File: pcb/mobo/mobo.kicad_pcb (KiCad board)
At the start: 2 copper layers, 51.6 x 89 mm, 69 parts, among them J1 SWD_10, J2 PEEL_MOTOR, J3 DRIVE_MOTOR, J4 SW1, J5 SPRING_FINGERS, J6 SW2, J7 SW1, J8 USART1, J9 SWD_10, U1 STM32F031C6Tx, U2 STM32F031K6Ux, U4 AP1117-33, U5 MC34063AD, U6 MAX3078E, U7 DRV8837, U8 DRV8837, Y1 8MHz

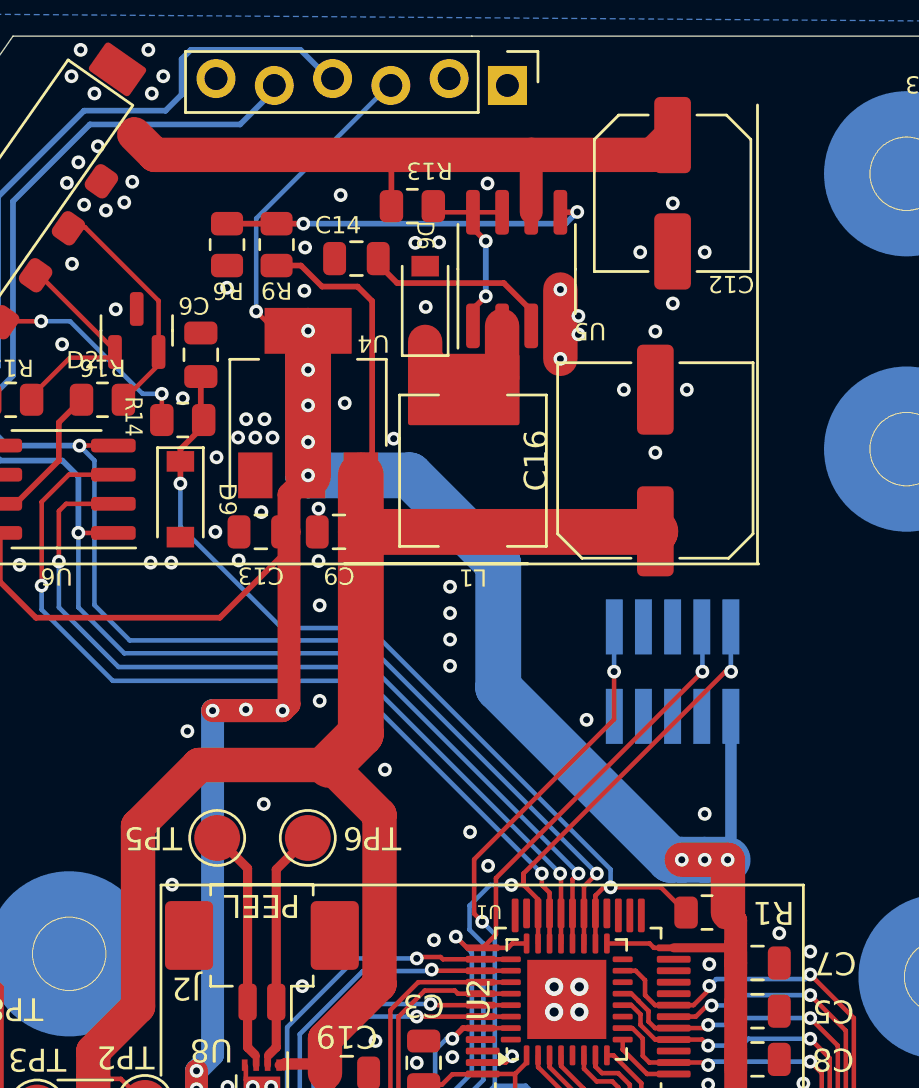
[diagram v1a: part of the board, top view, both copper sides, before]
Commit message: Convert SWD connector on back to TC2030. Left one on front for Adafruit 5434 connector.
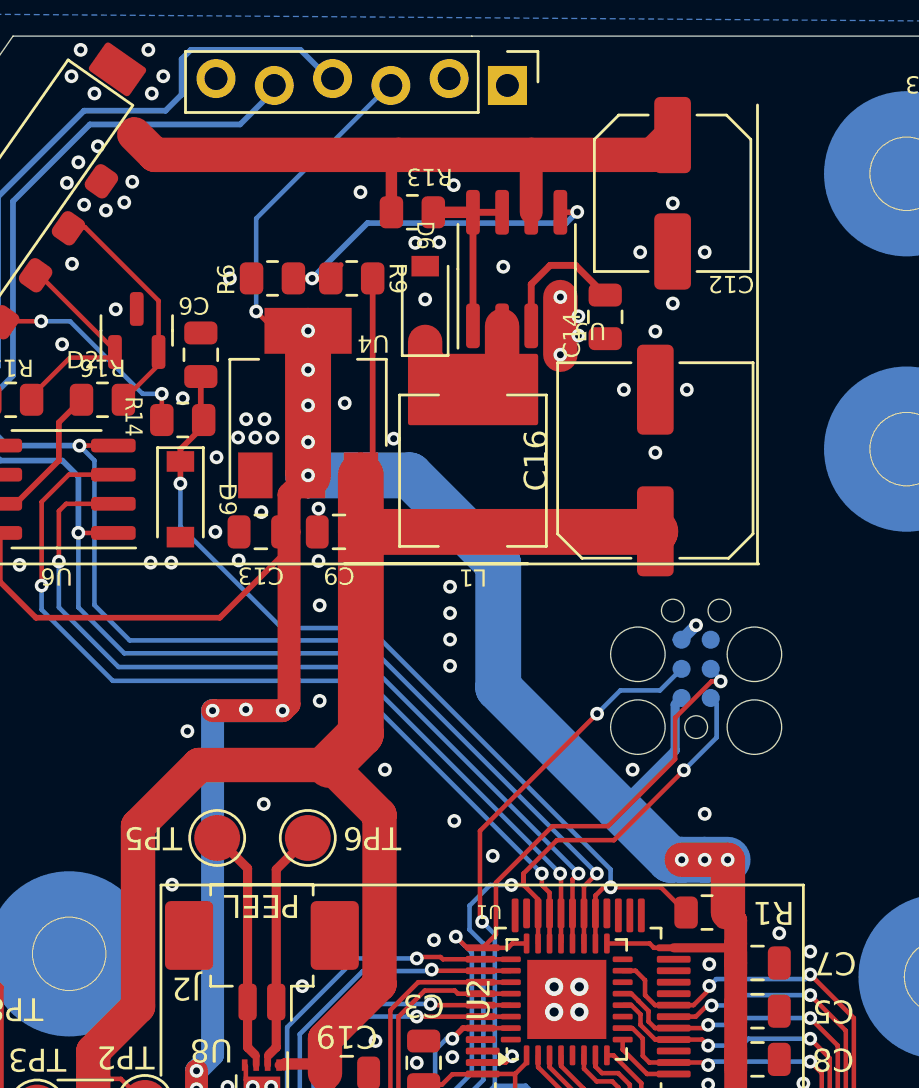
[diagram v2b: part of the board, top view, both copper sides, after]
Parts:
- J1: footprint Connector_PinHeader_1.27mm:PinHeader_2x05_P1.27mm_Vertical_SMD -> Connector:Tag-Connect_TC2030-IDC-FP_2x03_P1.27mm_Vertical
- moved C14 11.1 mm to (132.7, 42.0), turned to 90 degrees
- moved R9 3.59 mm to (121.6, 40.4), turned to 0 degrees
- moved R6 2.47 mm to (118.2, 40.4), turned to 180 degrees
- moved J1 1.03 mm to (136.6, 57.4)
- moved R13 0.27 mm to (124.3, 37.5)
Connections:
- J1 pad 3: GND -> RESET
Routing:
- net +10V: track 85.9 -> 82.1 mm
- net Net-(U5-TC): track 8.42 -> 5.92 mm
- net SWDIO: track 50.4 -> 48.5 mm
- net Net-(U5-Vfb): track 16.2 -> 15.2 mm
- net GND: track 42.7 -> 43.4 mm
- net Net-(U5-DC): track 8.52 -> 8.33 mm, vias 2 -> 0

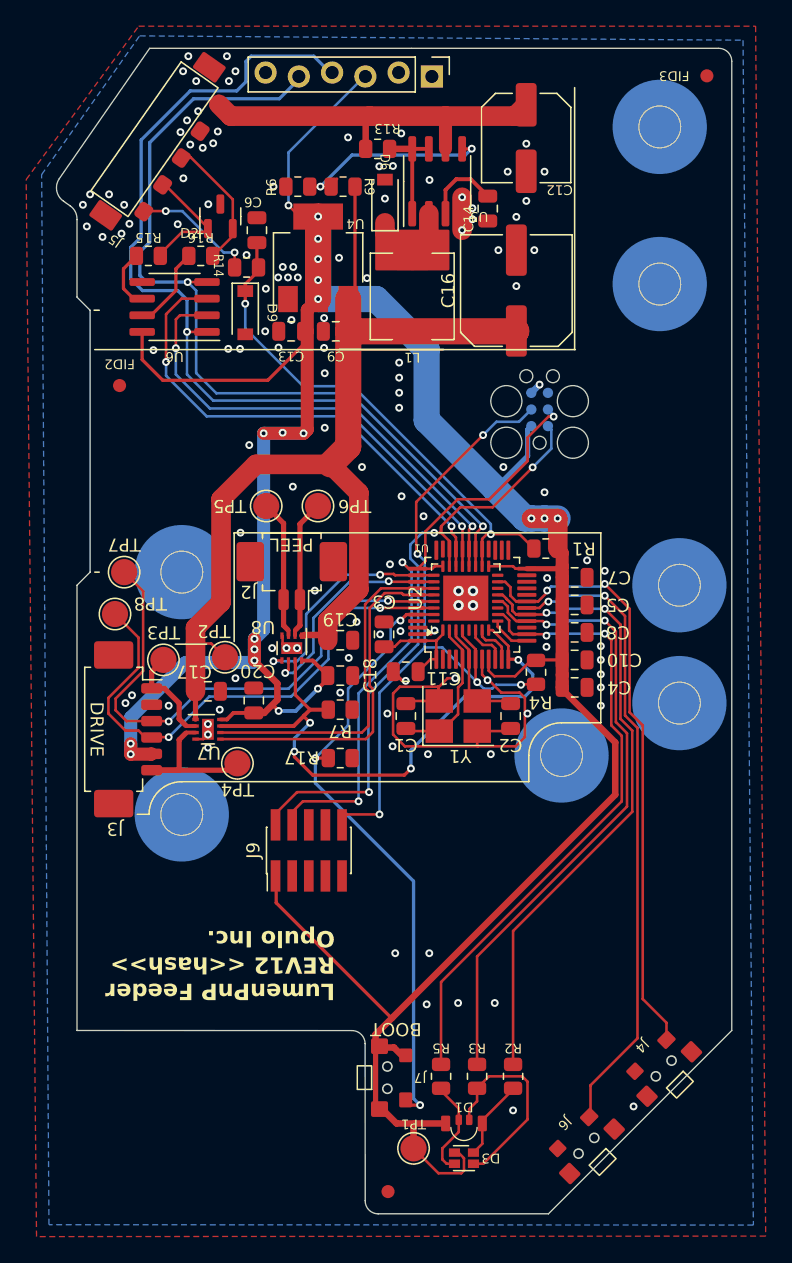
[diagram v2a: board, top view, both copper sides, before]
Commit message: Modify SWD footprint to make compatible with Adafruit 5434
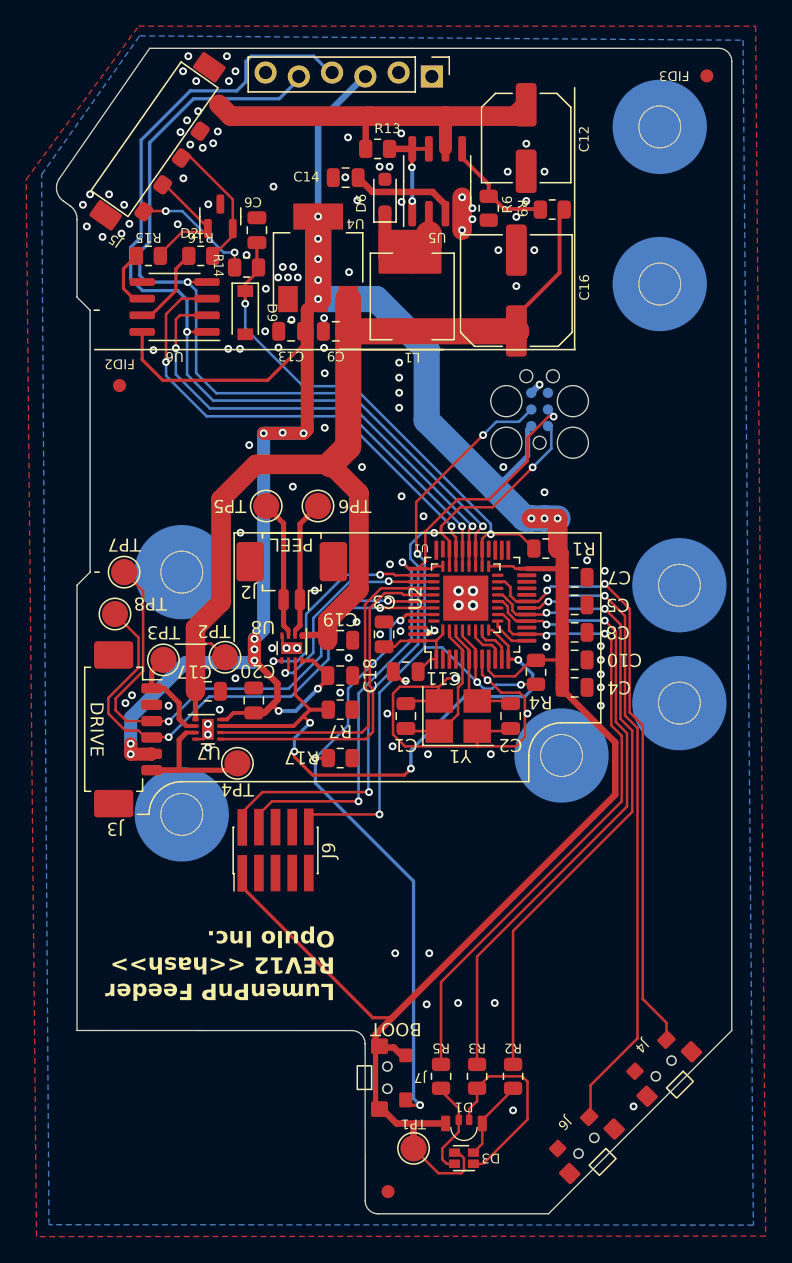
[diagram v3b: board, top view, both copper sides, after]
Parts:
- D6: footprint Diode_SMD:D_SOD-123 -> Diode_SMD:D_SOD-323_HandSoldering
- moved R9 16.1 mm to (137.6, 42.1)
- moved R6 14.7 mm to (132.7, 42.0), turned to -90 degrees
- moved C14 11.1 mm to (121.8, 39.7), turned to 0 degrees
- moved J9 2.54 mm to (116.5, 91.0)
- moved D6 0.43 mm to (124.8, 41.1)
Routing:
- net Net-(U5-Vfb): track 15.2 -> 8.82 mm, vias 2 -> 0
- net +10V: track 82.1 -> 84.8 mm
- net SWDIO: track 48.5 -> 51.1 mm
- net RESET: track 55.1 -> 57.7 mm
- net SWCLK: track 48.3 -> 50.7 mm
- net Net-(U5-TC): track 5.92 -> 8.20 mm
- net +3V3: track 257.5 -> 257.8 mm, vias 19 -> 18
- net Net-(U5-DC): track 8.33 -> 8.35 mm, vias 0 -> 2
